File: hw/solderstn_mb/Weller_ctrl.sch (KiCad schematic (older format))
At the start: 6 parts, among them U1301 TMUX1219, U1302 TMUX1219

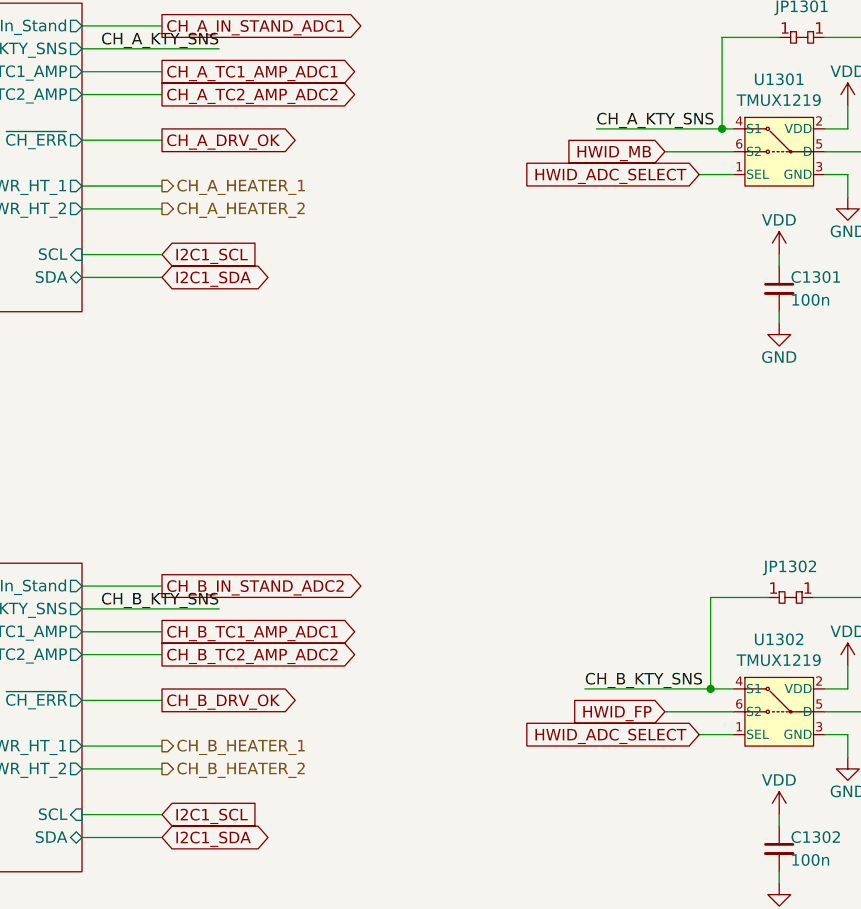
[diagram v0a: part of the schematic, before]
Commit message: Update pinout to "alternative", shuffling stuff around to optionally support a 2nd rotary on front-panel (corresponding Front-panel side not yet updated)
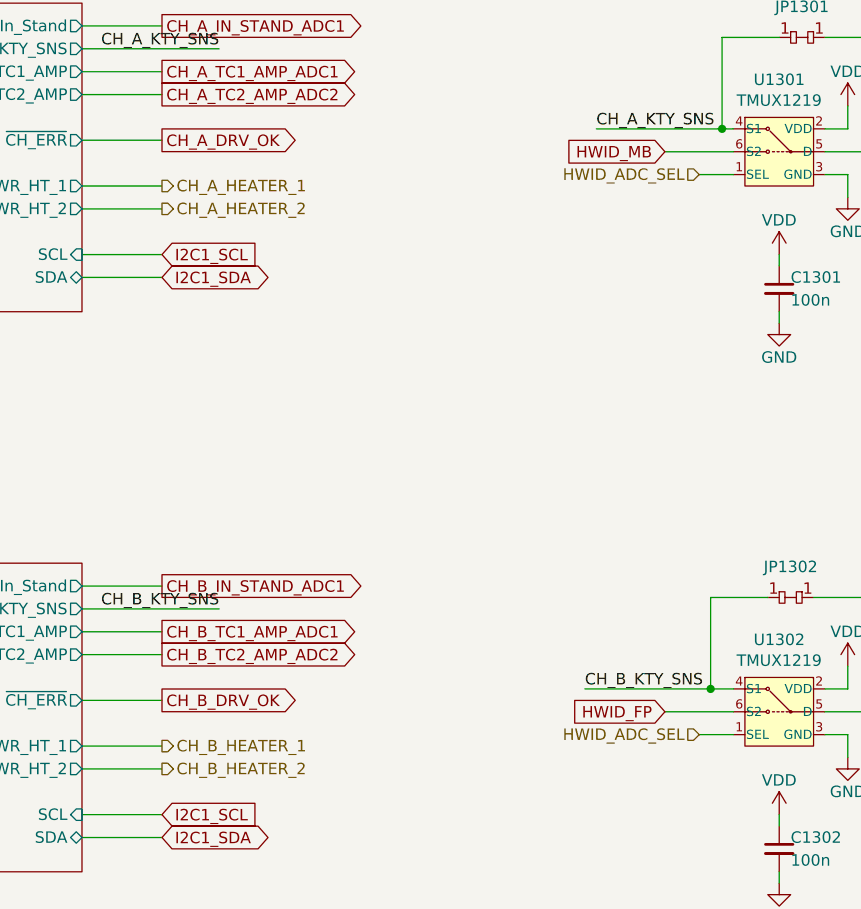
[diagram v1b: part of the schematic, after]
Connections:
- net HWID_ADC_SELECT renamed HWID_ADC_SEL
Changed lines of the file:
@@
 	6600 5350 6250 5350
 Text GLabel 6600 4850 2    50   Output ~ 0
-CH_B_IN_STAND_ADC2
+CH_B_IN_STAND_ADC1
 Text GLabel 6600 5050 2    50   Output ~ 0
 CH_B_TC1_AMP_ADC1
@@
 Wire Wire Line
 	9600 2850 9600 2750
-Text GLabel 8950 3050 0    50   Input ~ 0
-HWID_ADC_SELECT
 Wire Wire Line
 	9100 3050 8950 3050
-Text GLabel 8950 5500 0    50   Input ~ 0
-HWID_ADC_SELECT
 Wire Wire Line
 	9100 5500 8950 5500
@@
 Wire Wire Line
 	9750 5400 9500 5400
+Text HLabel 8950 3050 0    50   Input ~ 0
+HWID_ADC_SEL
+Text HLabel 8950 5500 0    50   Input ~ 0
+HWID_ADC_SEL
 $EndSCHEMATC

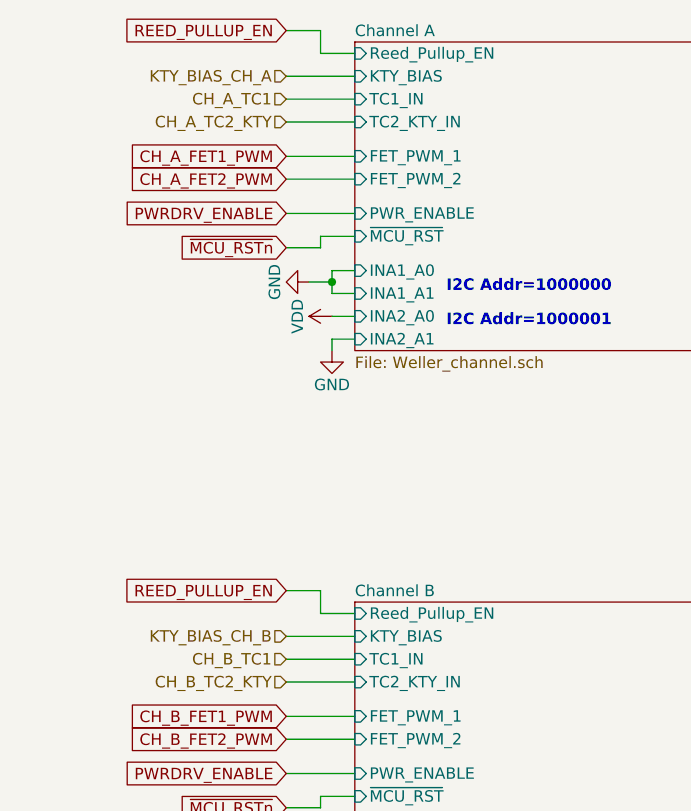
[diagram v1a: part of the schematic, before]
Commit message: * Remove separate REED_PULLUP_EN pin; instead bias the Reedswitches with the per-channel KTY bias (buffered Vref) * Add separate mini cut-out sub-PCB for 3.5 headphone connector at back-panel (must be angled vertical to fit in panel) * Some ESD and buffering on back panel
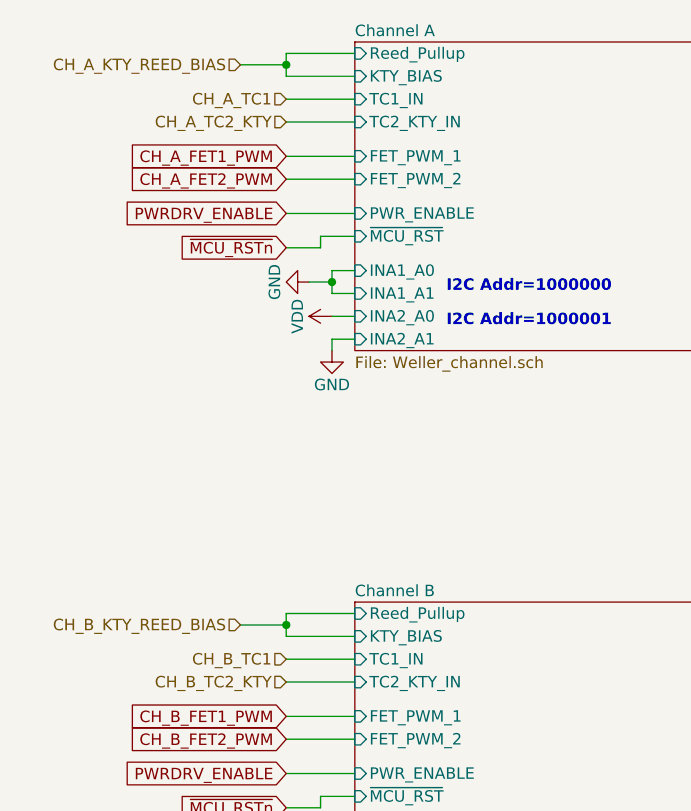
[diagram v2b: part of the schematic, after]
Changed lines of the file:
@@
 $Descr A4 11693 8268
 encoding utf-8
-Sheet 13 21
+Sheet 13 22
 Title "Dual Weller WMRP or WMRT capable channels"
 Date "2020-08-07"
@@
 F0 "Channel A" 50
 F1 "Weller_channel.sch" 50
-F2 "Reed_Pullup_EN" I L 4200 2350 50
-F3 "In_Stand" O R 6250 2400 50
-F4 "TC1_IN" I L 4200 2550 50
-F5 "KTY_BIAS" I L 4200 2450 50
-F6 "TC2_KTY_IN" I L 4200 2650 50
-F7 "TC1_AMP" O R 6250 2600 50
-F8 "TC2_AMP" O R 6250 2700 50
-F9 "INA1_A0" I L 4200 3300 50
-F10 "INA1_A1" I L 4200 3400 50
-F11 "SDA" B R 6250 3500 50
-F12 "SCL" I R 6250 3400 50
-F13 "INA2_A0" I L 4200 3500 50
-F14 "INA2_A1" I L 4200 3600 50
-F15 "PWR_ENABLE" I L 4200 3050 50
-F16 "FET_PWM_1" I L 4200 2800 50
-F17 "FET_PWM_2" I L 4200 2900 50
-F18 "~MCU_RST~" I L 4200 3150 50
-F19 "~CH_ERR~" O R 6250 2900 50
-F20 "PWR_HT_1" O R 6250 3100 50
-F21 "PWR_HT_2" O R 6250 3200 50
-F22 "KTY_SNS" O R 6250 2500 50
+F2 "In_Stand" O R 6250 2400 50
+F3 "TC1_IN" I L 4200 2550 50
+F4 "KTY_BIAS" I L 4200 2450 50
+F5 "TC2_KTY_IN" I L 4200 2650 50
+F6 "TC1_AMP" O R 6250 2600 50
+F7 "TC2_AMP" O R 6250 2700 50
+F8 "INA1_A0" I L 4200 3300 50
+F9 "INA1_A1" I L 4200 3400 50
+F10 "SDA" B R 6250 3500 50
+F11 "SCL" I R 6250 3400 50
+F12 "INA2_A0" I L 4200 3500 50
+F13 "INA2_A1" I L 4200 3600 50
+F14 "PWR_ENABLE" I L 4200 3050 50
+F15 "FET_PWM_1" I L 4200 2800 50
+F16 "FET_PWM_2" I L 4200 2900 50
+F17 "~MCU_RST~" I L 4200 3150 50
+F18 "~CH_ERR~" O R 6250 2900 50
+F19 "PWR_HT_1" O R 6250 3100 50
+F20 "PWR_HT_2" O R 6250 3200 50
+F21 "KTY_SNS" O R 6250 2500 50
+F22 "Reed_Pullup" I L 4200 2350 50
 $EndSheet
 $Sheet
@@
 F0 "Channel B" 50
 F1 "Weller_channel.sch" 50
-F2 "Reed_Pullup_EN" I L 4200 4800 50
-F3 "In_Stand" O R 6250 4850 50
-F4 "TC1_IN" I L 4200 5000 50
-F5 "KTY_BIAS" I L 4200 4900 50
-F6 "TC2_KTY_IN" I L 4200 5100 50
-F7 "TC1_AMP" O R 6250 5050 50
-F8 "TC2_AMP" O R 6250 5150 50
-F9 "INA1_A0" I L 4200 5750 50
-F10 "INA1_A1" I L 4200 5850 50
-F11 "SDA" B R 6250 5950 50
-F12 "SCL" I R 6250 5850 50
-F13 "INA2_A0" I L 4200 5950 50
-F14 "INA2_A1" I L 4200 6050 50
-F15 "PWR_ENABLE" I L 4200 5500 50
-F16 "FET_PWM_1" I L 4200 5250 50
-F17 "FET_PWM_2" I L 4200 5350 50
-F18 "~MCU_RST~" I L 4200 5600 50
-F19 "~CH_ERR~" O R 6250 5350 50
-F20 "PWR_HT_1" O R 6250 5550 50
-F21 "PWR_HT_2" O R 6250 5650 50
-F22 "KTY_SNS" O R 6250 4950 50
+F2 "In_Stand" O R 6250 4850 50
+F3 "TC1_IN" I L 4200 5000 50
+F4 "KTY_BIAS" I L 4200 4900 50
+F5 "TC2_KTY_IN" I L 4200 5100 50
+F6 "TC1_AMP" O R 6250 5050 50
+F7 "TC2_AMP" O R 6250 5150 50
+F8 "INA1_A0" I L 4200 5750 50
+F9 "INA1_A1" I L 4200 5850 50
+F10 "SDA" B R 6250 5950 50
+F11 "SCL" I R 6250 5850 50
+F12 "INA2_A0" I L 4200 5950 50
+F13 "INA2_A1" I L 4200 6050 50
+F14 "PWR_ENABLE" I L 4200 5500 50
+F15 "FET_PWM_1" I L 4200 5250 50
+F16 "FET_PWM_2" I L 4200 5350 50
+F17 "~MCU_RST~" I L 4200 5600 50
+F18 "~CH_ERR~" O R 6250 5350 50
+F19 "PWR_HT_1" O R 6250 5550 50
+F20 "PWR_HT_2" O R 6250 5650 50
+F21 "KTY_SNS" O R 6250 4950 50
+F22 "Reed_Pullup" I L 4200 4800 50
 $EndSheet
-Text HLabel 3900 2450 0    50   Input ~ 0
-KTY_BIAS_CH_A
-Text HLabel 3900 4900 0    50   Input ~ 0
-KTY_BIAS_CH_B
+Text HLabel 3700 2400 0    50   Input ~ 0
+CH_A_KTY_REED_BIAS
+Text HLabel 3700 4850 0    50   Input ~ 0
+CH_B_KTY_REED_BIAS
 Wire Wire Line
 	4200 2450 3900 2450
@@
 Wire Wire Line
 	3900 5100 4200 5100
-Text GLabel 3900 2250 0    50   Input ~ 0
-REED_PULLUP_EN
-Wire Wire Line
-	3900 2250 4050 2250
-Wire Wire Line
-	4050 2250 4050 2350
-Wire Wire Line
-	4050 2350 4200 2350
-Text GLabel 3900 4700 0    50   Input ~ 0
-REED_PULLUP_EN
-Wire Wire Line
-	3900 4700 4050 4700
-Wire Wire Line
-	4050 4700 4050 4800
-Wire Wire Line
-	4050 4800 4200 4800
 Text GLabel 3900 2800 0    50   Input ~ 0
 CH_A_FET1_PWM
@@
 Text HLabel 8950 5500 0    50   Input ~ 0
 HWID_ADC_SEL
+Wire Wire Line
+	3900 4900 3900 4850
+Wire Wire Line
+	3900 4800 4200 4800
+Wire Wire Line
+	3900 2450 3900 2400
+Wire Wire Line
+	3900 2350 4200 2350
+Wire Wire Line
+	3700 2400 3900 2400
+Connection ~ 3900 2400
+Wire Wire Line
+	3900 2400 3900 2350
+Wire Wire Line
+	3700 4850 3900 4850
+Connection ~ 3900 4850
+Wire Wire Line
+	3900 4850 3900 4800
 $EndSCHEMATC

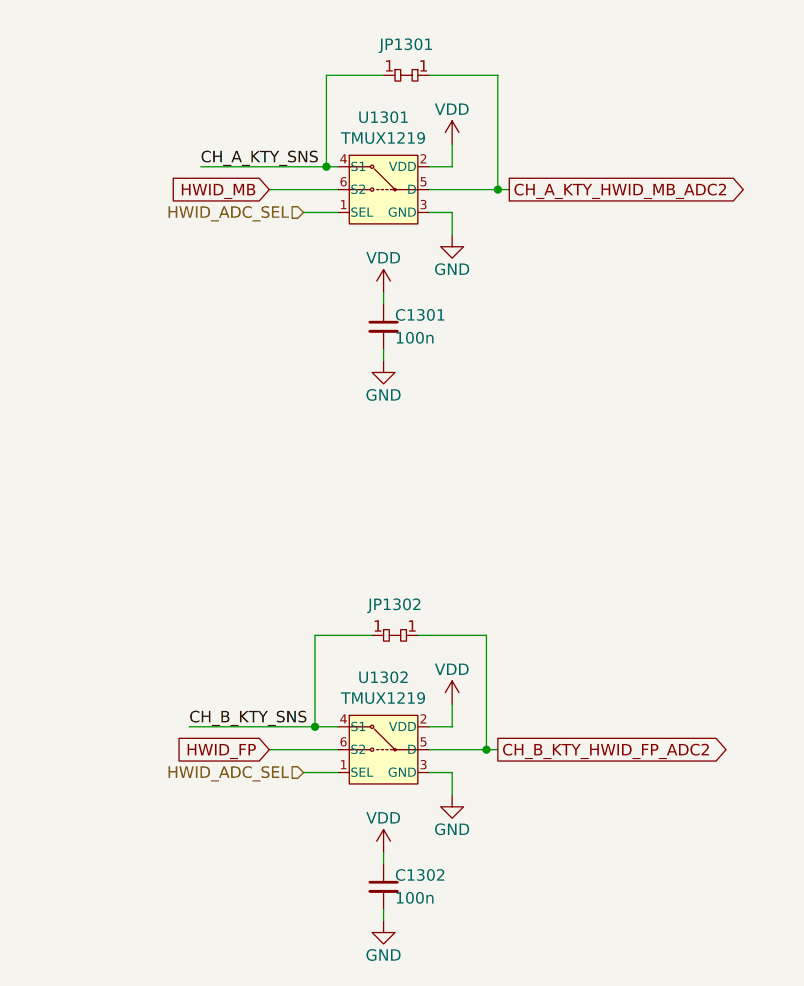
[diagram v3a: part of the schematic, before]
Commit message: Updated display-board sch & PCB with optional left-hand rotary encoder instead of pwrbtn. Printed MB schematic updates PDF for 20-08-21
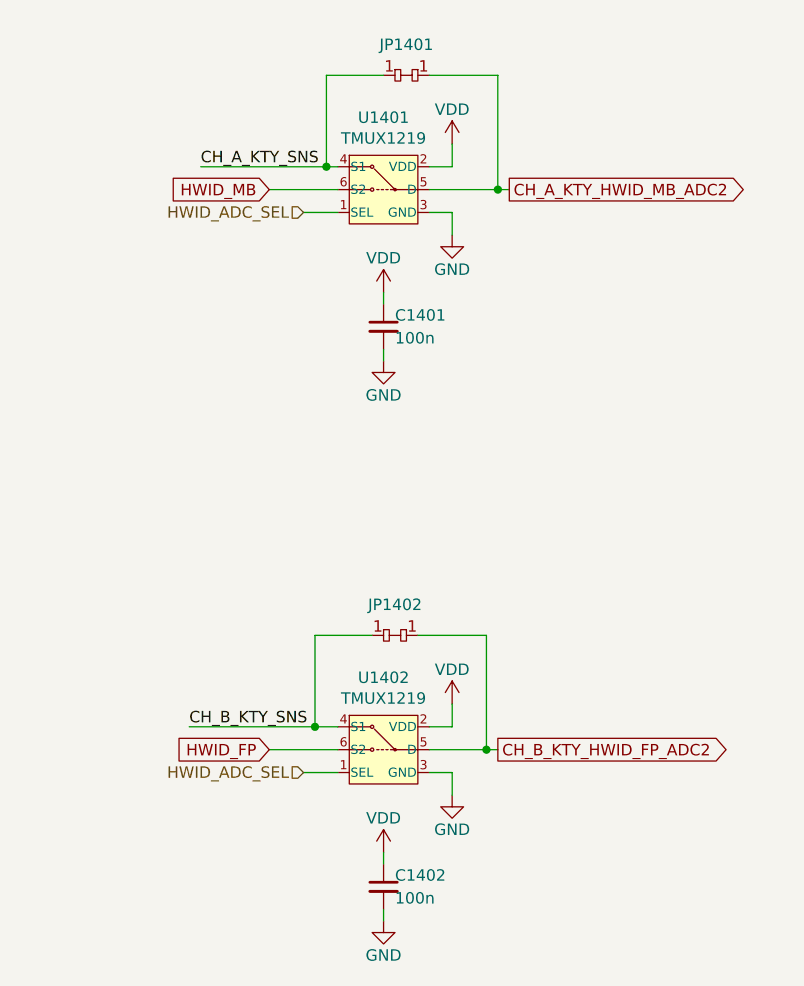
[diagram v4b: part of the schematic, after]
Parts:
- renumbered C1301 to C1401, C1302 to C1402, JP1301 to JP1401, JP1302 to JP1402, U1301 to U1401, U1302 to U1402
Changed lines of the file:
@@
 	6600 5950 6250 5950
 $Comp
-L power:VDD #PWR01305
+L power:VDD #PWR01405
 U 1 1 5FD719AC
 P 4100 3500
-F 0 "#PWR01305" H 4100 3350 50  0001 C CNN
+F 0 "#PWR01405" H 4100 3350 50  0001 C CNN
 F 1 "VDD" H 4100 3650 50  0000 C CNN
 F 2 "" H 4100 3500 50  0001 C CNN
@@
 $EndComp
 $Comp
-L power:GND #PWR01306
+L power:GND #PWR01406
 U 1 1 5FD71E70
 P 4100 3650
-F 0 "#PWR01306" H 4100 3400 50  0001 C CNN
+F 0 "#PWR01406" H 4100 3400 50  0001 C CNN
 F 1 "GND" H 4100 3500 50  0000 C CNN
 F 2 "" H 4100 3650 50  0001 C CNN
@@
 $EndComp
 $Comp
-L power:GND #PWR01303
+L power:GND #PWR01403
 U 1 1 5FD72072
 P 4000 3350
-F 0 "#PWR01303" H 4000 3100 50  0001 C CNN
+F 0 "#PWR01403" H 4000 3100 50  0001 C CNN
 F 1 "GND" H 4000 3200 50  0000 C CNN
 F 2 "" H 4000 3350 50  0001 C CNN
@@
 	4100 3500 4200 3500
 $Comp
-L power:GND #PWR01310
+L power:GND #PWR01410
 U 1 1 5FD784C8
 P 4100 5750
-F 0 "#PWR01310" H 4100 5500 50  0001 C CNN
+F 0 "#PWR01410" H 4100 5500 50  0001 C CNN
 F 1 "GND" H 4100 5600 50  0000 C CNN
 F 2 "" H 4100 5750 50  0001 C CNN
@@
 $EndComp
 $Comp
-L power:VDD #PWR01313
+L power:VDD #PWR01413
 U 1 1 5FD78863
 P 4000 6000
-F 0 "#PWR01313" H 4000 5850 50  0001 C CNN
+F 0 "#PWR01413" H 4000 5850 50  0001 C CNN
 F 1 "VDD" H 4000 6150 50  0000 C CNN
 F 2 "" H 4000 6000 50  0001 C CNN
@@
 	4100 6000 4100 6050
 $Comp
-L power:VDD #PWR01311
+L power:VDD #PWR01411
 U 1 1 5FD7B8CF
 P 3900 5850
-F 0 "#PWR01311" H 3900 5700 50  0001 C CNN
+F 0 "#PWR01411" H 3900 5700 50  0001 C CNN
 F 1 "VDD" H 3900 6000 50  0000 C CNN
 F 2 "" H 3900 5850 50  0001 C CNN
@@
 CH_B_KTY_SNS
 $Comp
-L customlib_mj:TMUX1219 U1301
+L customlib_mj:TMUX1219 U1401
 U 1 1 5F6627CA
 P 9300 2950
-F 0 "U1301" H 9300 3265 50  0000 C CNN
+F 0 "U1401" H 9300 3265 50  0000 C CNN
 F 1 "TMUX1219" H 9300 3174 50  0000 C CNN
 F 2 "Package_TO_SOT_SMD:SOT-23-6_Handsoldering" H 9300 2950 50  0001 C CNN
@@
 $EndComp
 $Comp
-L customlib_mj:TMUX1219 U1302
+L customlib_mj:TMUX1219 U1402
 U 1 1 5F663745
 P 9300 5400
-F 0 "U1302" H 9300 5715 50  0000 C CNN
+F 0 "U1402" H 9300 5715 50  0000 C CNN
 F 1 "TMUX1219" H 9300 5624 50  0000 C CNN
 F 2 "Package_TO_SOT_SMD:SOT-23-6_Handsoldering" H 9300 5400 50  0001 C CNN
@@
 	9800 5400 9750 5400
 $Comp
-L power:GND #PWR01309
+L power:GND #PWR01409
 U 1 1 5F66CC03
 P 9600 5600
-F 0 "#PWR01309" H 9600 5350 50  0001 C CNN
+F 0 "#PWR01409" H 9600 5350 50  0001 C CNN
 F 1 "GND" H 9600 5450 50  0000 C CNN
 F 2 "" H 9600 5600 50  0001 C CNN
@@
 $EndComp
 $Comp
-L power:GND #PWR01302
+L power:GND #PWR01402
 U 1 1 5F66D2FE
 P 9600 3150
-F 0 "#PWR01302" H 9600 2900 50  0001 C CNN
+F 0 "#PWR01402" H 9600 2900 50  0001 C CNN
 F 1 "GND" H 9600 3000 50  0000 C CNN
 F 2 "" H 9600 3150 50  0001 C CNN
@@
 $EndComp
 $Comp
-L power:VDD #PWR01301
+L power:VDD #PWR01401
 U 1 1 5F66EADD
 P 9600 2750
-F 0 "#PWR01301" H 9600 2600 50  0001 C CNN
+F 0 "#PWR01401" H 9600 2600 50  0001 C CNN
 F 1 "VDD" H 9600 2900 50  0000 C CNN
 F 2 "" H 9600 2750 50  0001 C CNN
@@
 $EndComp
 $Comp
-L power:VDD #PWR01308
+L power:VDD #PWR01408
 U 1 1 5F66FA33
 P 9600 5200
-F 0 "#PWR01308" H 9600 5050 50  0001 C CNN
+F 0 "#PWR01408" H 9600 5050 50  0001 C CNN
 F 1 "VDD" H 9600 5350 50  0000 C CNN
 F 2 "" H 9600 5200 50  0001 C CNN
@@
 	9100 5500 8950 5500
 $Comp
-L Device:C_Small C1302
+L Device:C_Small C1402
 U 1 1 5F67D632
 P 9300 6000
-F 0 "C1302" H 9350 6050 50  0000 L CNN
+F 0 "C1402" H 9350 6050 50  0000 L CNN
 F 1 "100n" H 9350 5950 50  0000 L CNN
 F 2 "" H 9300 6000 50  0001 C CNN
@@
 $EndComp
 $Comp
-L power:VDD #PWR01312
+L power:VDD #PWR01412
 U 1 1 5F67DC46
 P 9300 5850
-F 0 "#PWR01312" H 9300 5700 50  0001 C CNN
+F 0 "#PWR01412" H 9300 5700 50  0001 C CNN
 F 1 "VDD" H 9300 6000 50  0000 C CNN
 F 2 "" H 9300 5850 50  0001 C CNN
@@
 $EndComp
 $Comp
-L power:GND #PWR01314
+L power:GND #PWR01414
 U 1 1 5F67DF5D
 P 9300 6150
-F 0 "#PWR01314" H 9300 5900 50  0001 C CNN
+F 0 "#PWR01414" H 9300 5900 50  0001 C CNN
 F 1 "GND" H 9300 6000 50  0000 C CNN
 F 2 "" H 9300 6150 50  0001 C CNN
@@
 	9300 6100 9300 6150
 $Comp
-L Device:C_Small C1301
+L Device:C_Small C1401
 U 1 1 5F681CF8
 P 9300 3550
-F 0 "C1301" H 9350 3600 50  0000 L CNN
+F 0 "C1401" H 9350 3600 50  0000 L CNN
 F 1 "100n" H 9350 3500 50  0000 L CNN
 F 2 "" H 9300 3550 50  0001 C CNN
@@
 $EndComp
 $Comp
-L power:VDD #PWR01304
+L power:VDD #PWR01404
 U 1 1 5F681D02
 P 9300 3400
-F 0 "#PWR01304" H 9300 3250 50  0001 C CNN
+F 0 "#PWR01404" H 9300 3250 50  0001 C CNN
 F 1 "VDD" H 9300 3550 50  0000 C CNN
 F 2 "" H 9300 3400 50  0001 C CNN
@@
 $EndComp
 $Comp
-L power:GND #PWR01307
+L power:GND #PWR01407
 U 1 1 5F681D0C
 P 9300 3700
-F 0 "#PWR01307" H 9300 3450 50  0001 C CNN
+F 0 "#PWR01407" H 9300 3450 50  0001 C CNN
 F 1 "GND" H 9300 3550 50  0000 C CNN
 F 2 "" H 9300 3700 50  0001 C CNN
@@
 	9300 3650 9300 3700
 $Comp
-L customlib_mj:dogbone_2 JP1301
+L customlib_mj:dogbone_2 JP1401
 U 1 1 5F686AB5
 P 9400 2450
-F 0 "JP1301" H 9400 2584 50  0000 C CNN
+F 0 "JP1401" H 9400 2584 50  0000 C CNN
 F 1 "dogbone_2" H 9400 2550 50  0001 C CNN
 F 2 "customlib_mj_fp:db2_0402" H 9400 2450 50  0001 C CNN
@@
 	9800 2950 9500 2950
 $Comp
-L customlib_mj:dogbone_2 JP1302
+L customlib_mj:dogbone_2 JP1402
 U 1 1 5F692262
 P 9350 4900
-F 0 "JP1302" H 9350 5034 50  0000 C CNN
+F 0 "JP1402" H 9350 5034 50  0000 C CNN
 F 1 "dogbone_2" H 9350 5000 50  0001 C CNN
 F 2 "customlib_mj_fp:db2_0402" H 9350 4900 50  0001 C CNN
